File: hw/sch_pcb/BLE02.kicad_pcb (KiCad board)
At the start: 2 copper layers, 40.1 x 30 mm, 42 parts, among them J1 Conn_Coaxial, J2 3.3-5V, J3 JUMP_5X2, J4 JUMP_5X2, M1 HOLE, M2 HOLE, M3 HOLE, M4 HOLE, U1 TXS0104EPW, U2 CC2564CRVMR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

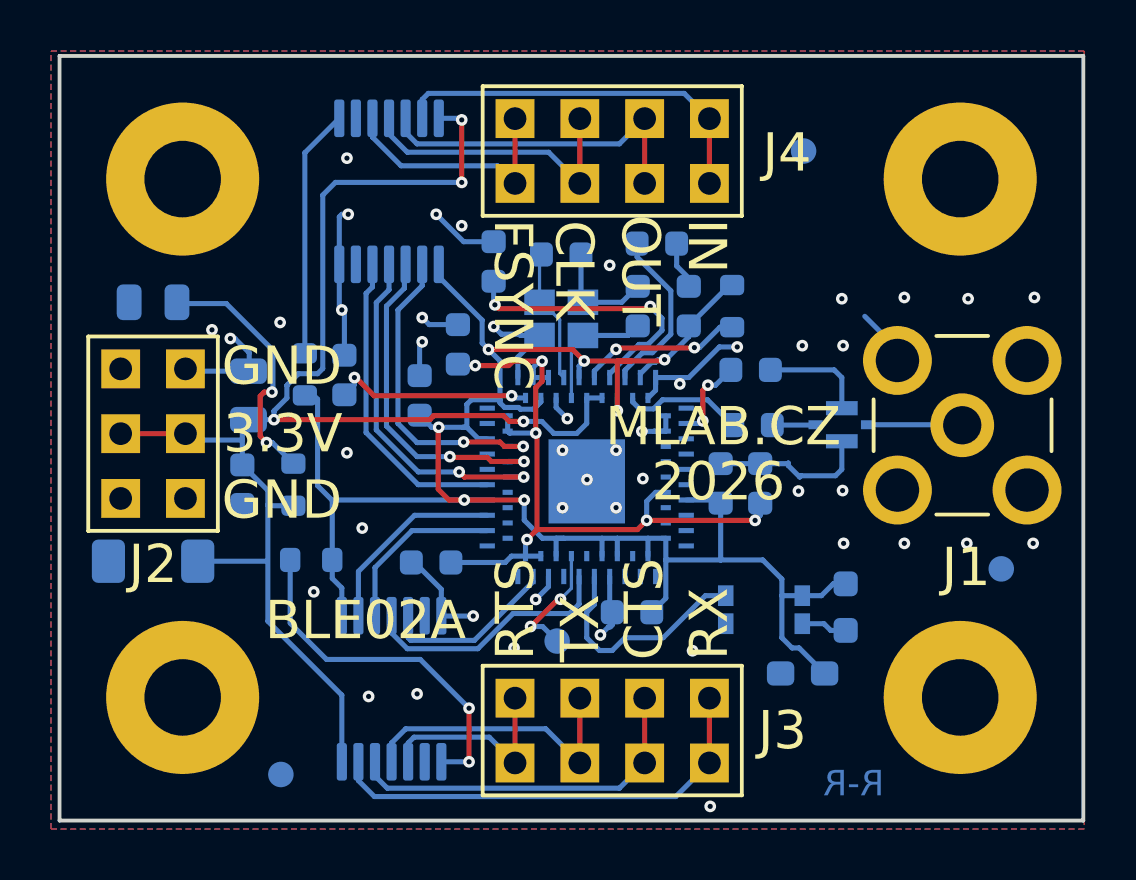
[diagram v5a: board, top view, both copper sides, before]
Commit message: Cleanup layout. Fix obsolete part types.
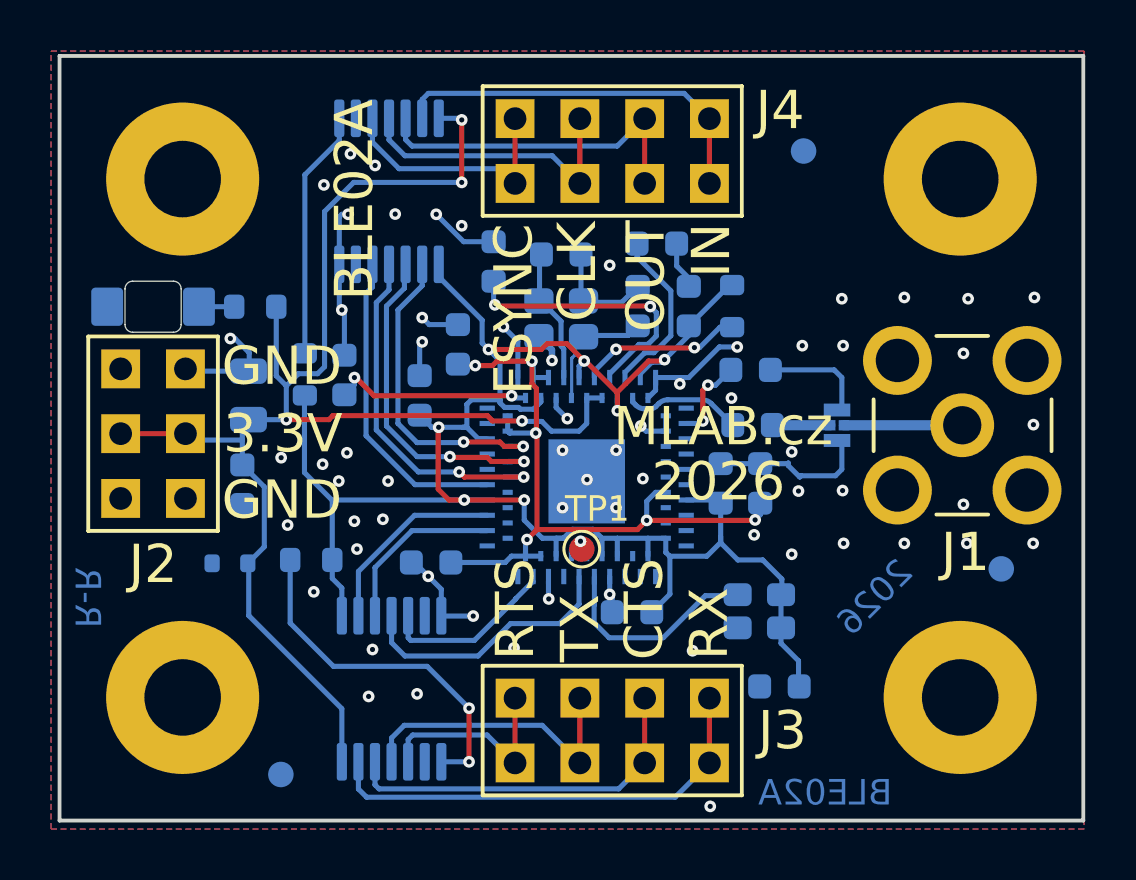
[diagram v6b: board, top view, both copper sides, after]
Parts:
- removed FL1: DEA202450BT-1213C1, cc2654-board-footprints:DEA202450BT-1213C1
- removed R5: 10k, Resistor_SMD:R_0603_1608Metric_Pad0.98x0.95mm_HandSolder
- removed X1: ASH7K-32.768KHZ-T, MLAB_Lib:ASH7K_ABR
- added U4: LFB212G45CG1C187, MLAB_SAW:Murata_C187, B.Cu at (158.9, 104.5)
- added Y1: LFSPXO009682, Oscillator:Oscillator_SMD_SeikoEpson_SG210-4Pin_2.5x2.0mm, B.Cu at (155.9, 111.8)
- C8: footprint Capacitor_SMD:C_0603_1608Metric_Pad1.08x0.95mm_HandSolder -> Capacitor_SMD:C_0603_1608Metric
- D1: footprint LED_SMD:LED_0805_2012Metric -> Mlab_D:LED_1206_mill
- D3: value BZV55C-6,2V -> BZX585-B5V6.115; footprint Diode_SMD:D_MiniMELF -> Diode_SMD:D_SOD-523
- J2: value 3.3-5V -> 3.3V
- TP1: moved to F.Cu
- U2: footprint MLAB_Lib:RVM0076A -> Mlab_IO:RVM0076A
- Y3: footprint cc2654-board-footprints:XTAL_ECS-260-8-36CKM-TR -> Crystal:Crystal_SMD_2520-4Pin_2.5x2.0mm
- moved R4 7.13 mm to (136.1, 99.8), turned to 180 degrees
- moved TP1 3.73 mm to (148.9, 109.3)
- moved D3 3.02 mm to (135.1, 109.9)
- moved C8 1.04 mm to (156.7, 114.7)
- moved D1 0.17 mm to (132.1, 99.8), turned to 180 degrees
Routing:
- net Net-(D1-A): track 9.77 -> 1.38 mm, vias 2 -> 0
- net Net-(U2A-TX_DBG): track 4.77 -> 0.67 mm, vias 2 -> 1
- net GND: track 52.4 -> 49.0 mm, vias 45 -> 63
- net VDD_1V8: track 78.9 -> 76.0 mm
- net Net-(X1-VIO): track 1.81 -> 0.00 mm
- net BT_SLOW_CLK: track 9.07 -> 7.90 mm
- net Net-(J1-In): track 3.82 -> 4.64 mm
- net Net-(U1-B4): track 9.62 -> 8.92 mm
- net Net-(C1-Pad1): track 29.2 -> 28.6 mm
- net VCC: track 57.9 -> 57.3 mm
- net Net-(U4-IN): track 1.68 -> 2.27 mm
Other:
- board text added: "MLAB.cz"
- board text removed: "MLAB.CZ"
